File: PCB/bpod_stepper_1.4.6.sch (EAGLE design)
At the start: 29 parts, among them IC1 LM3480-5.0, IC2 SN65HVD31DR, IC3 MCP1792, IC4 MCP1793_SOT223-5, J8 POWER_JACK

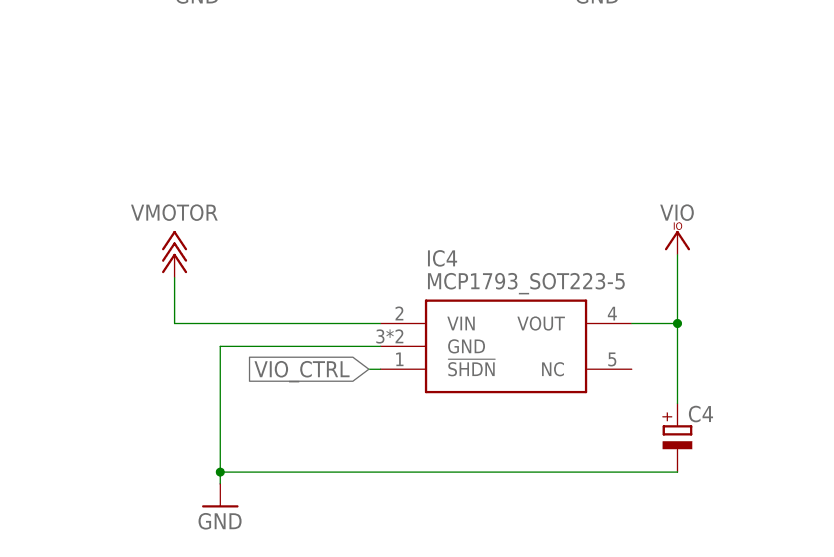
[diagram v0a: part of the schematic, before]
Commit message: added D12 to prevent current flowing from pin 28 to pin 4
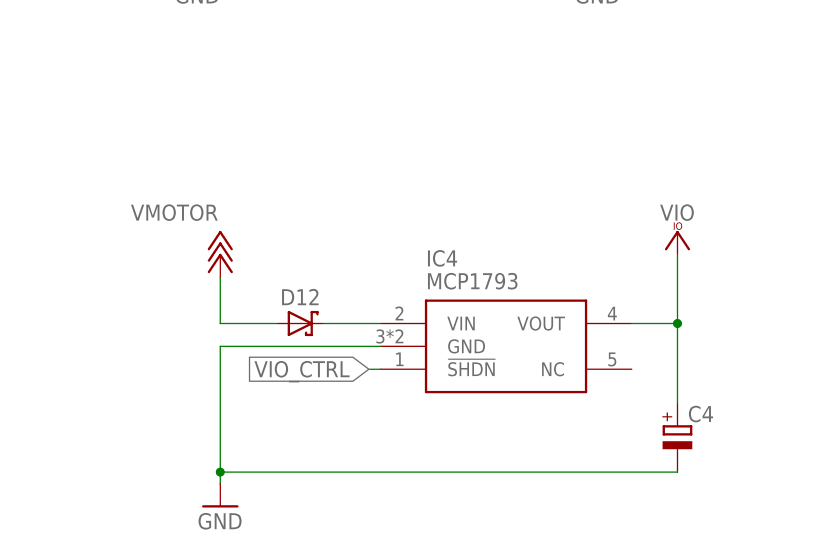
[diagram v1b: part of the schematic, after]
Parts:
- added D12: S310FA, we-rcl:D_SCHOTTKY-SOD123
- IC4: value MCP1793_SOT223-5 -> MCP1793
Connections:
- new net N$1: D12.C, IC4.VIN
- net VMOTOR: now also D12.A; no longer IC4.VIN
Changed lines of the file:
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@@
 <part name="SUPPLY1" library="supply1" library_urn="urn:adsk.eagle:library:371" deviceset="+18V" device=""/>
 <part name="VCC2" library="supply1" library_urn="urn:adsk.eagle:library:371" deviceset="VCCIO" device=""/>
-<part name="IC4" library="MCP1793" deviceset="MCP1793_SOT223-5" device=""/>
+<part name="IC4" library="MCP1793" deviceset="MCP1793_SOT223-5" device="" value="MCP1793"/>
 <part name="C4" library="rcl" library_urn="urn:adsk.eagle:library:334" deviceset="CPOL-EU" device="B" package3d_urn="urn:adsk.eagle:package:23421/2"/>
 <part name="C3" library="rcl" library_urn="urn:adsk.eagle:library:334" deviceset="CPOL-EU" device="B" package3d_urn="urn:adsk.eagle:package:23421/2"/>
+<part name="D12" library="we-rcl" deviceset="D_SCHOTTKY" device="-SOD123" value="S310FA"/>
 </parts>
 <sheets>
@@
 <attribute name="VALUE" x="76.2" y="7.62" size="1.778" layer="96"/>
 </instance>
-<instance part="SUPPLY1" gate="1" x="73.66" y="38.1" smashed="yes"/>
+<instance part="SUPPLY1" gate="1" x="78.74" y="38.1" smashed="yes"/>
 <instance part="VCC2" gate="G$1" x="129.54" y="40.64" smashed="yes"/>
 <instance part="IC4" gate="G$1" x="111.76" y="27.94" smashed="yes">
@@
 <attribute name="NAME" x="79.883" y="151.6126" size="1.778" layer="95"/>
 <attribute name="VALUE" x="79.883" y="146.5326" size="1.778" layer="96"/>
+</instance>
+<instance part="D12" gate="D" x="87.63" y="30.48" smashed="yes">
+<attribute name="NAME" x="87.63" y="32.512" size="1.778" layer="95" align="bottom-center"/>
 </instance>
 </instances>
@@
 </segment>
 <segment>
-<wire x1="73.66" y1="35.56" x2="73.66" y2="30.48" width="0.1524" layer="91"/>
+<wire x1="78.74" y1="35.56" x2="78.74" y2="30.48" width="0.1524" layer="91"/>
 <pinref part="SUPPLY1" gate="1" pin="+18V"/>
 <label x="73.66" y="41.91" size="1.778" layer="95" align="bottom-center"/>
-<pinref part="IC4" gate="G$1" pin="VIN"/>
-<wire x1="96.52" y1="30.48" x2="73.66" y2="30.48" width="0.1524" layer="91"/>
+<pinref part="D12" gate="D" pin="A"/>
+<wire x1="78.74" y1="30.48" x2="85.09" y2="30.48" width="0.1524" layer="91"/>
 </segment>
 </net>
@@
 </segment>
 </net>
+<net name="N$1" class="0">
+<segment>
+<pinref part="D12" gate="D" pin="C"/>
+<pinref part="IC4" gate="G$1" pin="VIN"/>
+<wire x1="90.17" y1="30.48" x2="96.52" y2="30.48" width="0.1524" layer="91"/>
+</segment>
+</net>
